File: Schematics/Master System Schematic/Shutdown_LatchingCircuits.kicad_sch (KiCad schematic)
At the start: 8 parts, among them K501 Omron DPDT Relay, K502 Omron DPDT Relay, K503 Omron DPDT Relay, K504 Omron DPDT Relay

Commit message: Updated all + annotations
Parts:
- renumbered D501 to D8, D502 to D9, K501 to K1, K502 to K2, K503 to K3, K504 to K4, R501 to R2, R502 to R3
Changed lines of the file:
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@@
   (symbol (lib_id "Relay:G5V-2") (at 186.69 123.19 270) (unit 1)
     (in_bom yes) (on_board yes)
-    (property "Reference" "K504" (id 0) (at 186.69 103.7082 90))
+    (property "Reference" "K4" (id 0) (at 186.69 103.7082 90))
     (property "Value" "Omron DPDT Relay" (id 1) (at 186.69 106.0196 90))
     (property "Footprint" "Relay_THT:Relay_DPDT_Omron_G5V-2" (id 2) (at 185.42 139.7 0)
@@
   (symbol (lib_id "Relay:G5V-2") (at 186.69 67.31 270) (mirror x) (unit 1)
     (in_bom yes) (on_board yes)
-    (property "Reference" "K503" (id 0) (at 186.69 86.7918 90))
+    (property "Reference" "K3" (id 0) (at 186.69 86.7918 90))
     (property "Value" "Omron DPDT Relay" (id 1) (at 186.69 84.4804 90))
     (property "Footprint" "Relay_THT:Relay_DPDT_Omron_G5V-2" (id 2) (at 185.42 50.8 0)
@@
   (symbol (lib_id "Diode:1N4001") (at 186.69 96.52 0) (unit 1)
     (in_bom yes) (on_board yes)
-    (property "Reference" "D502" (id 0) (at 186.69 91.0336 0))
+    (property "Reference" "D9" (id 0) (at 186.69 91.0336 0))
     (property "Value" "1N4001" (id 1) (at 186.69 93.345 0))
     (property "Footprint" "Diode_THT:D_DO-41_SOD81_P10.16mm_Horizontal" (id 2) (at 186.69 100.965 0)
@@
   (symbol (lib_id "Relay:G5V-2") (at 106.68 123.19 270) (unit 1)
     (in_bom yes) (on_board yes)
-    (property "Reference" "K502" (id 0) (at 106.68 103.7082 90))
+    (property "Reference" "K2" (id 0) (at 106.68 103.7082 90))
     (property "Value" "Omron DPDT Relay" (id 1) (at 106.68 106.0196 90))
     (property "Footprint" "Relay_THT:Relay_DPDT_Omron_G5V-2" (id 2) (at 105.41 139.7 0)
@@
   (symbol (lib_id "Relay:G5V-2") (at 106.68 67.31 270) (mirror x) (unit 1)
     (in_bom yes) (on_board yes)
-    (property "Reference" "K501" (id 0) (at 106.68 86.7918 90))
+    (property "Reference" "K1" (id 0) (at 106.68 86.7918 90))
     (property "Value" "Omron DPDT Relay" (id 1) (at 106.68 84.4804 90))
     (property "Footprint" "Relay_THT:Relay_DPDT_Omron_G5V-2" (id 2) (at 105.41 50.8 0)
@@
   (symbol (lib_id "Diode:1N4001") (at 106.68 96.52 0) (mirror y) (unit 1)
     (in_bom yes) (on_board yes)
-    (property "Reference" "D501" (id 0) (at 106.68 91.0336 0))
+    (property "Reference" "D8" (id 0) (at 106.68 91.0336 0))
     (property "Value" "1N4001" (id 1) (at 106.68 93.345 0))
     (property "Footprint" "Diode_THT:D_DO-41_SOD81_P10.16mm_Horizontal" (id 2) (at 106.68 100.965 0)
@@
   (symbol (lib_id "Device:R") (at 120.65 59.69 90) (unit 1)
     (in_bom yes) (on_board yes)
-    (property "Reference" "R501" (id 0) (at 120.65 57.15 90))
+    (property "Reference" "R2" (id 0) (at 120.65 57.15 90))
     (property "Value" "470" (id 1) (at 120.65 62.23 90))
     (property "Footprint" "" (id 2) (at 120.65 61.468 90)
@@
   (symbol (lib_id "Device:R") (at 201.93 59.69 90) (unit 1)
     (in_bom yes) (on_board yes)
-    (property "Reference" "R502" (id 0) (at 201.93 57.15 90))
+    (property "Reference" "R3" (id 0) (at 201.93 57.15 90))
     (property "Value" "470" (id 1) (at 201.93 62.23 90))
     (property "Footprint" "" (id 2) (at 201.93 61.468 90)

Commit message: Did a whole bunch of wire gauges and misc
Cleaned up runs
assigned wire gauges
implemented new glv/shutdown BRB placement design
updated some things in LV plate
started making names consistent
added new charger functionality in connector
left notes on some things to do
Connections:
- net GLV renamed ShutdownLatch_GLV+
- net Ground renamed GND
- net IMD_Latch_Reset+ renamed IMD_Fault
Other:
- note added: "Add CAN watch latching circuit"
- moved on the sheet: D8, D9, K1, K2, K3, K4, R2, R3

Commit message: Footwell integration fix (#113)
* Beginning footwell fix

adding in

* Finished box, doing celeanup

* Cleaning up can wires

* Added non critical power

* Added misc indicators

* replaced old chassis markers

* fixing pin input/output/passive status

* Consolidation (part 1)

* Consolidation (part 2)

* Consolidation part 3 complete

#Scope creep

* weird autosave issue

* Fixing pin directions and grounds

* adding notations

* Adding CAN latching circuitry

* Fixed pin directions, added can latch

* FINAL edits
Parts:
- added D?: 1N4001, Diode_THT:D_DO-41_SOD81_P10.16mm_Horizontal, symbol Diode:1N4001
- added K? (x2): Omron DPDT Relay, Relay_THT:Relay_DPDT_Omron_G5V-2, symbol Relay:G5V-2
- added R?: 470, symbol Device:R
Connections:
- net GND: now also D?.2 (A), K?.1, K?.1
- net Shutdown_IN renamed ShutdownLoop_IN
- net Shutdown_OUT: no longer names the net of K3.8
- net Shutdown_OUT: now also K?.4
- new net: K?.11, R?.1
- new net CAN_Fault: K?.4
- new net CAN_Fault_Indicator: R?.2
- new net CAN_Latch_Reset-: D?.1 (K), K?.16, K?.16, K?.8
- new net ShutdownLoop_OUT: K?.8
- no-connect marks 12 -> 18
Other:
- note removed: "Add CAN watch latching circuit"

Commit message: Dylan cleanup and continualupdates (#114)
* Annotations

* Added custom Chassis GND symbol
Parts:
- gave numbers to parts that had none: 4
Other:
- moved on the sheet: D15, D8, D9, K1, K10, K11, K2, K3, K4, R2, R3, R4

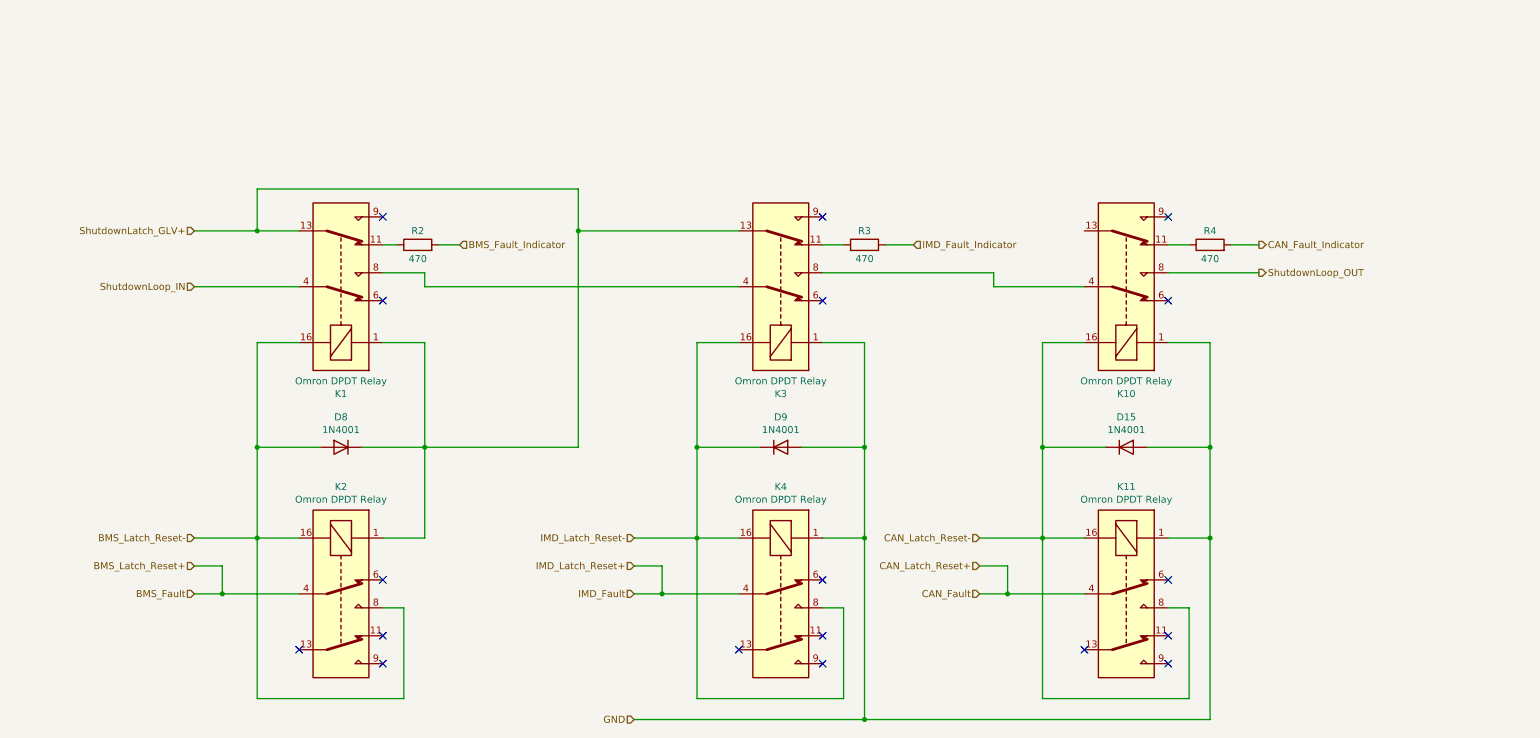
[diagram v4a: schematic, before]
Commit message: Added missing 12V in latching
Missing 12V to CAN fault pole
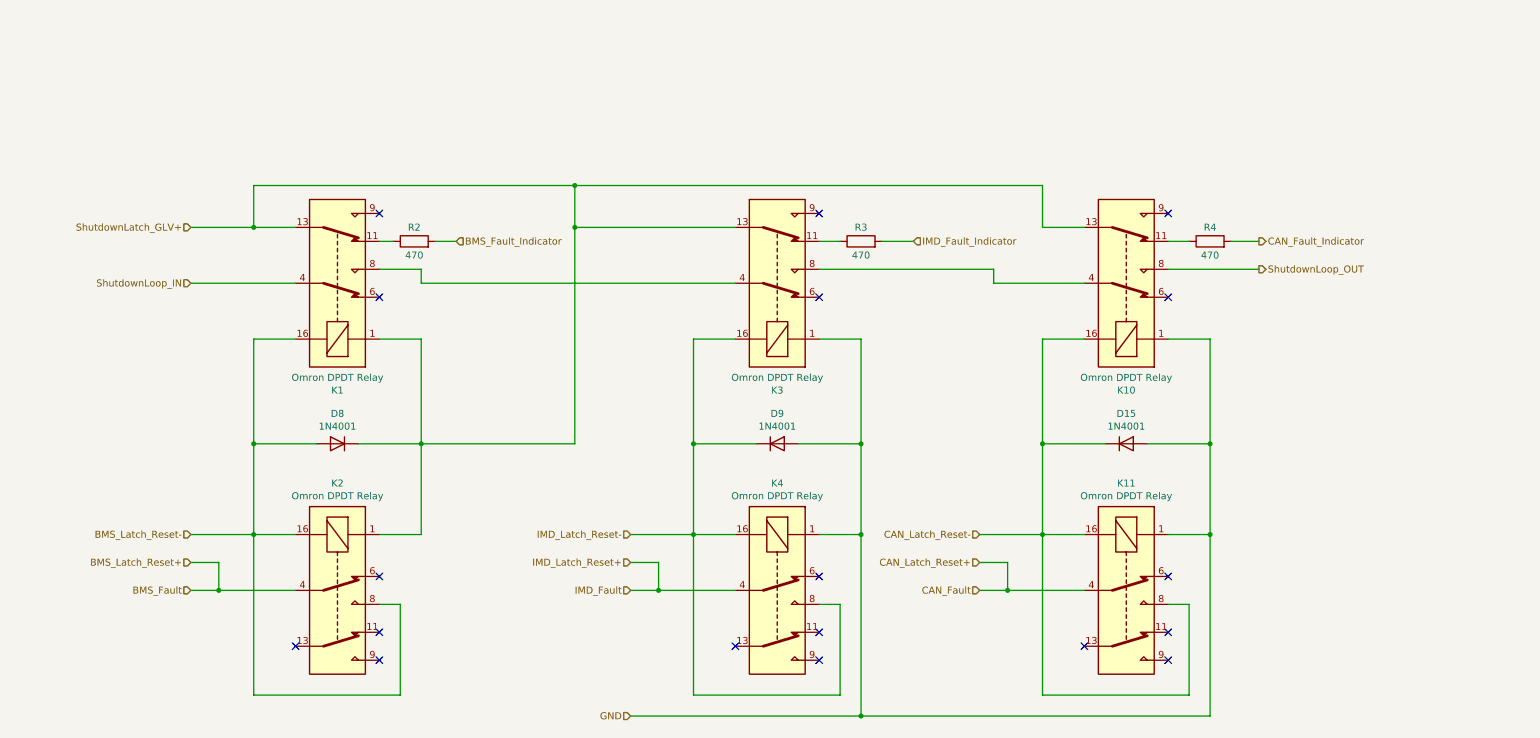
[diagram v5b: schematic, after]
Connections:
- net ShutdownLatch_GLV+: now also K10.13
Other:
- moved on the sheet: D15, D8, D9, K1, K10, K11, K2, K3, K4, R2, R3, R4
